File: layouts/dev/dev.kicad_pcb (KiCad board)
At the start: 6 copper layers, 32.5 x 59.6 mm, 85 parts

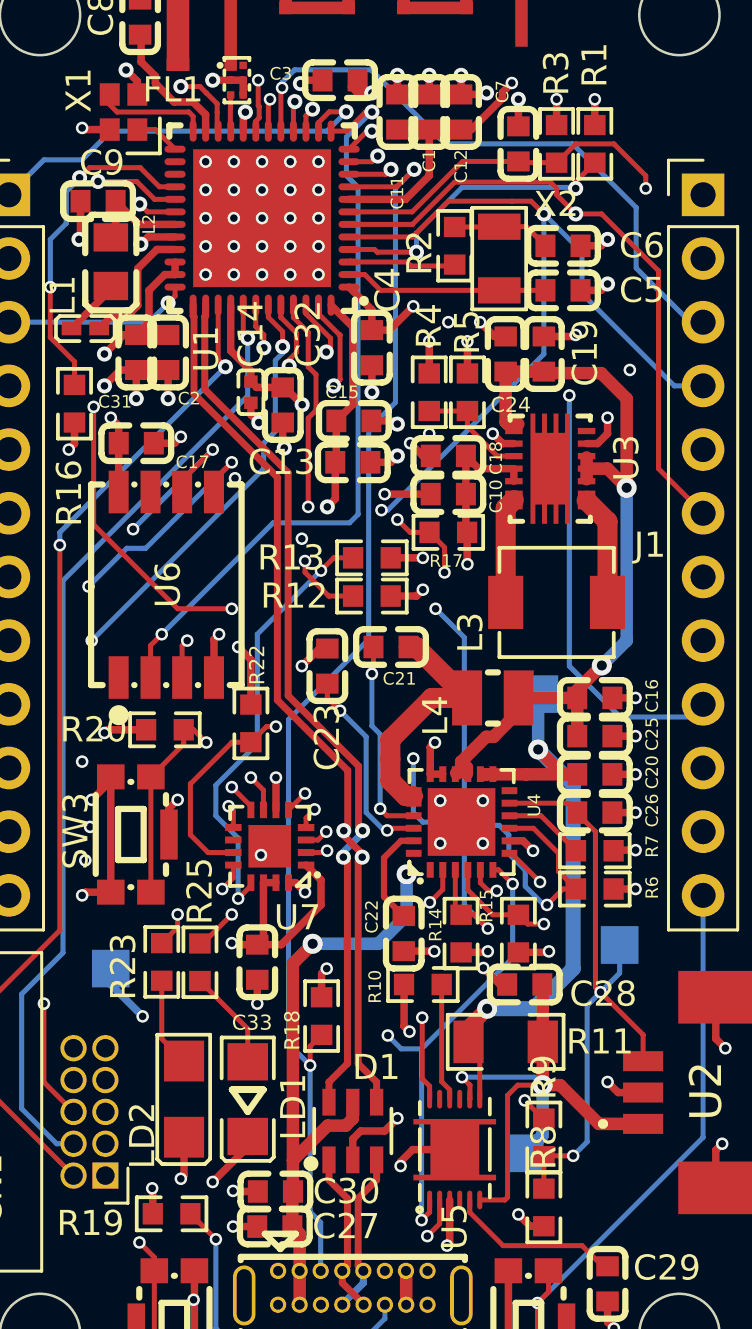
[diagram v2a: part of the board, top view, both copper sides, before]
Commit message: fix: stitch thermal pads by their real copper, not their bounding box
The TPS63020 and BQ27441 exposed pads were never stitched, and for the
whole project the tool reported them as "0.01 x 0.01 placeholders, not
thermal pads". That reading was wrong. Both are custom pads: 0.01 x 0.01 is
the anchor size and the real shape lives in the primitives. Measured on the
board they are 1.58 x 4.40 mm (6.95 mm2) and 3.30 x 2.45 mm (8.09 mm2),
both on F.Cu with paste and both on GND. The footprints were fine all
along; the tool could not see them because it read GetSizeX/GetSizeY.

Reading the bounding box instead fixes the detection and breaks two other
things, both of which surfaced immediately:

* the grid was computed in pad-local coordinates and then rotated, while
  the bounding box is already in board coordinates. On U3, rotated -90
  degrees, the axes swapped and two of four vias landed outside the pad,
  among the converter's lead pads.
* a bounding box is a rectangle and these pads are not. The BQ27441 pad is
  a T: a 2.0 x 1.95 mm centre bar plus two vertical strips 0.22 mm wide,
  where a 0.5 mm via can never fit. The TPS63020 pad is a comb. Gridding
  the rectangle puts vias on bare laminate.

So placement now works from the copper itself: candidates on a 0.1 mm
raster over the bounding box, each tested for whether the whole via -
centre and four points on its circumference - sits inside the pad polygon,
then picked greedily from the centre outwards with the pitch as the only
spacing rule.

The first run of that produced 18 shorts. A through via also pierces In2,
In3 and B.Cu, and the board had SD_CLK, SD_MISO, SD_MOSI, PB6, CHG_CE,
CHG_PG and GAUGE_INT routed under those parts. Every candidate is now also
checked against foreign copper on every layer, and the report says how many
positions that blocked - 673 under the MCU alone, which is why its grid
dropped from 27 vias to 19.

Zone filling moved into board_setup. The script adds and deletes vias, and
a pour fill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
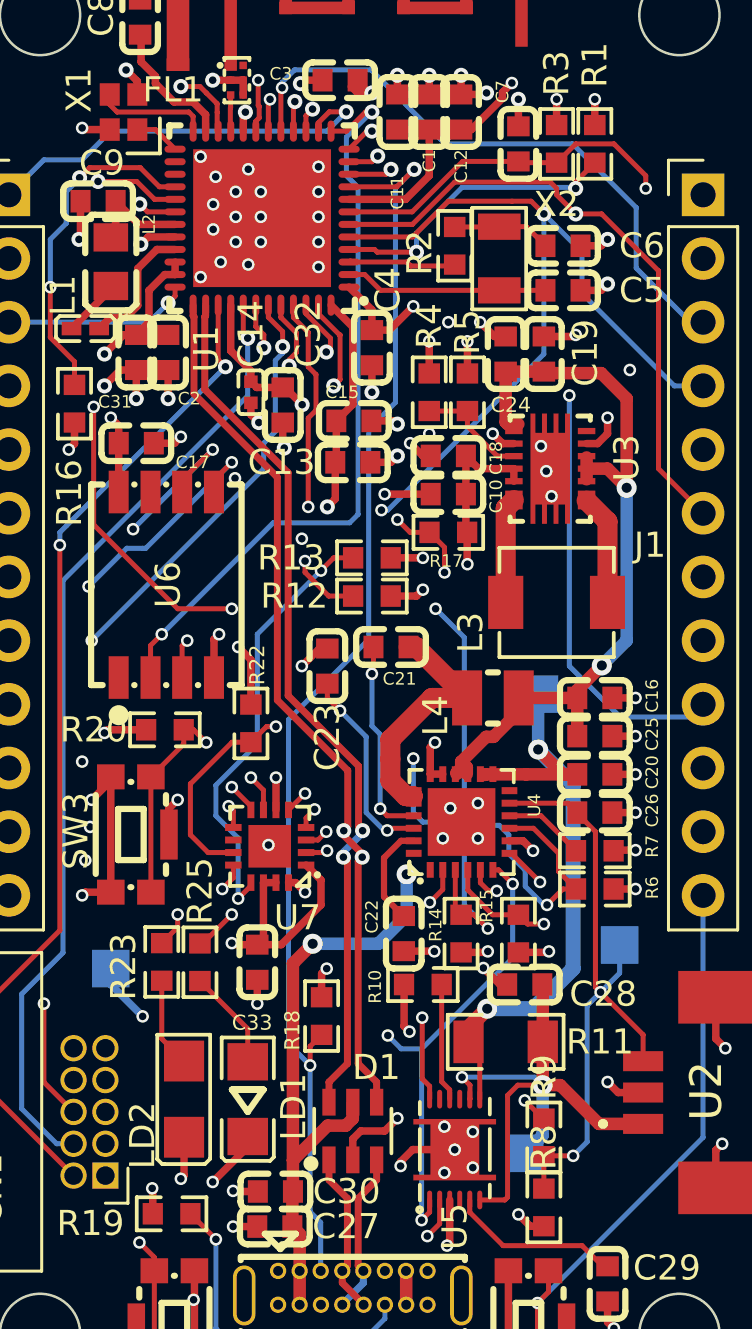
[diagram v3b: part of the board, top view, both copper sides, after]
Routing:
- net GND: vias 97 -> 99

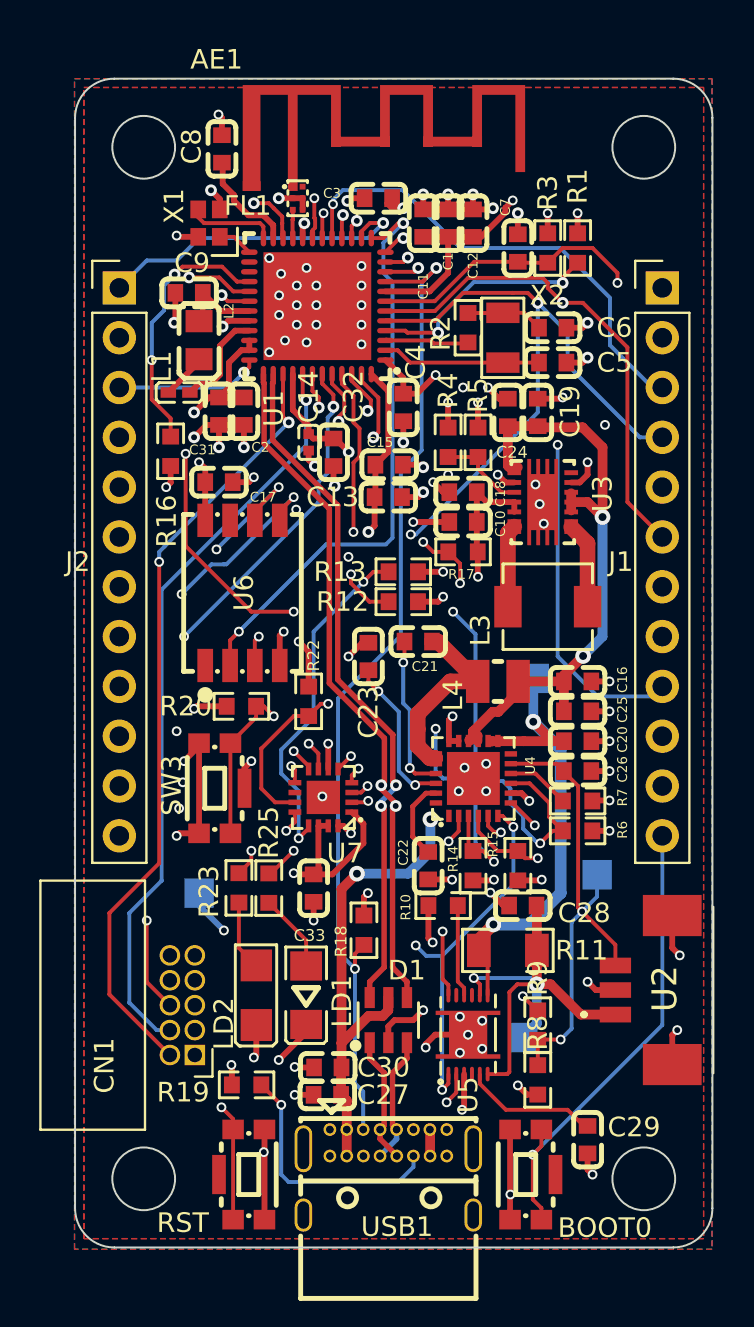
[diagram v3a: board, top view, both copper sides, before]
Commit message: feat: grow the board 1 mm upward and make the pours connect to pads
Two findings drove this, and the second one explains four unconnected
ground items at once.

The pours were set to ZONE_CONNECTION_NONE - all six of them, including the
In1 ground plane and the In4 power plane. A pour in that mode keeps
clearance from pads of its own net, so every ground pad without an explicit
track or via to it was left floating: the antenna's shorting stub, which is
the entire operating principle of an inverted-F; the MLPF's ground; and the
shields of both buttons. nowa_wylewka() has always set FULL, but set_zones
never corrected the pours it found, and that is the gap.

They are now forced to THT_THERMAL rather than FULL: solid for SMD pads,
thermal spokes for through-hole. This board is hand-soldered and a solid
ground connection on a header pin sinks heat faster than an iron delivers
it. F.Cu fragmentation dropped from 70 islands to 56.

Three islands still have no path to the plane - the antenna stub and the
two button shields. Each island is the pad itself with routing crowding it,
so the pour cannot physically reach, and none is large enough to hold a
0.5 mm via with clearance: 0.90 x 0.50, 0.71 x 1.89 and 0.59 x 1.89 against
the 0.80 mm a via needs in both axes. That is copper to be moved by hand,
not a setting.

The 1 mm comes off the top edge: BOARD_Y_MM 3.30 -> 2.30 with the height
59.60 -> 60.60, so the bottom edge and everything already placed stay put
and the space appears where it was needed. The top mounting holes follow to
y 5.80, the bottom pair stays at 59.40. For the antenna this is noise - the
counterpoise grows 1.7 % and was already twice a quarter wave at 2.45 GHz.

Keepout geometry was left alone after checking it: its lower edge sits
0.25 mm above the feed deliberately, because the two towers drop below it
into ground, which is where the shorting via belongs. The comment at
ANTENA_KEEPOUT_MM said so all along. The reason no via is there is simply
that the 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
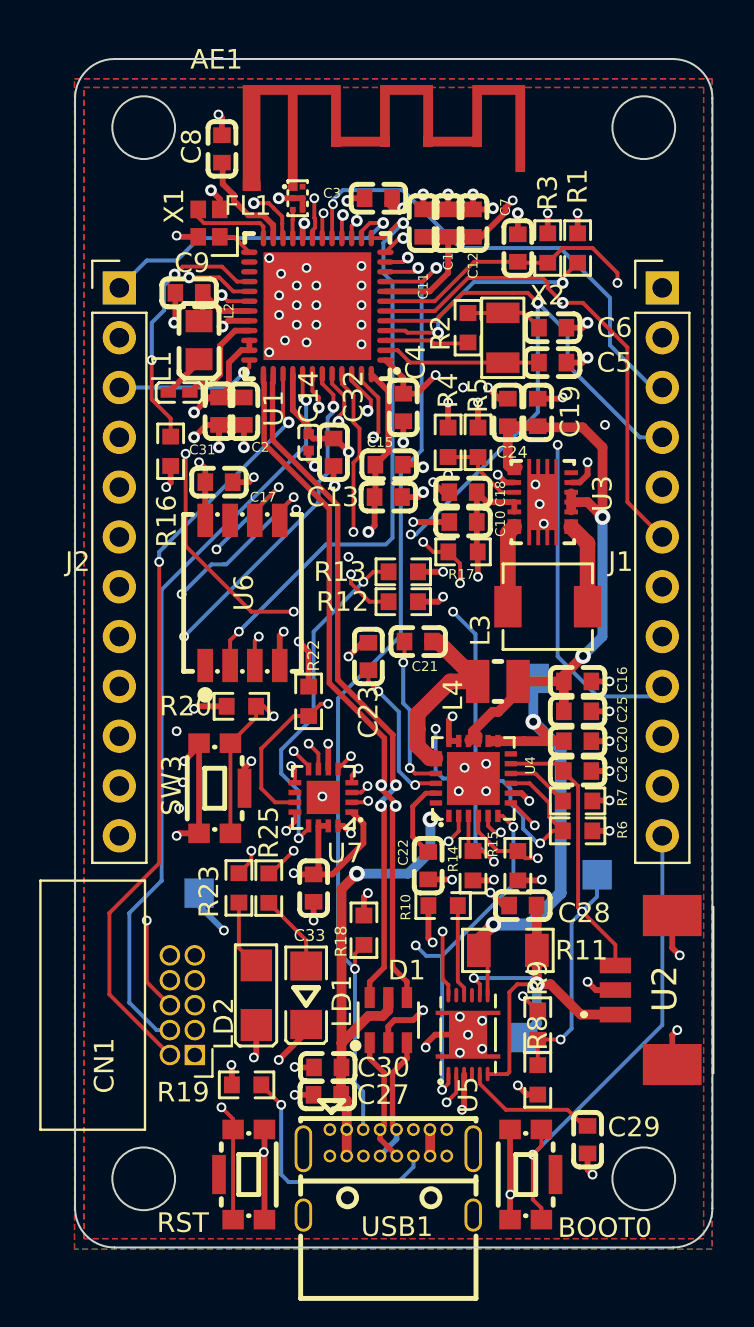
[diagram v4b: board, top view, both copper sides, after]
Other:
- board size 32.5 x 59.6 mm -> 32.5 x 60.6 mm

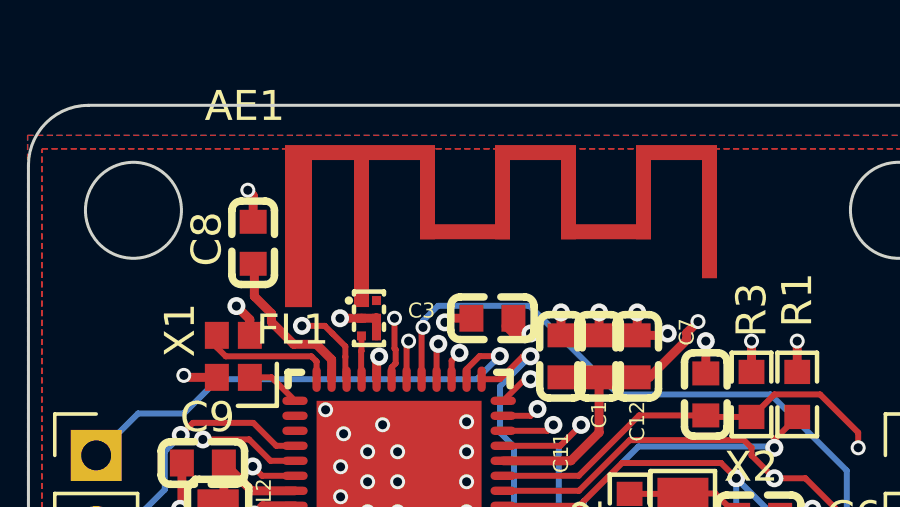
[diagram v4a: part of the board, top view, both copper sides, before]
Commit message: fix: give the antenna's shorting stub somewhere to land
The inverted-F had no DC path from its radiator to ground, which is not a
detail - the short to ground is the entire operating principle. Without it
the structure is a piece of copper at an undefined impedance.

The cause was dimensional. The comment at ANTENA_KEEPOUT_MM has always said
the two towers drop below the keepout into ground, "tam laduje przelotka
zwierajaca", so a shorting via was part of the design from the start. It was
never placed because it never could be: the stub foot from AN043 Table 1 is
0.90 x 0.50 mm and a 0.5 mm via with clearance needs 0.80 mm in both axes.

The footprint gains one rectangle that is not in Table 1: 1.10 x 1.10 mm
under the stub foot, at local (-2.10, +0.75) so it overlaps the foot and
merges with it. It sits below the keepout, already in ground territory, so
it is not part of the resonant structure - the note's warning that "small
changes of the antenna dimensions may have large impact on the performance"
is respected because no dimension from Table 1 was touched.

It started at 1.60 x 1.50 and had to come down to 1.10 x 1.10: at the larger
size it collided with the +3V3 tracks running left of the stub. 0.55 mm from
centre to edge against the 0.40 a via needs.

The antenna moved up 0.50 mm, not the full millimetre the new outline
offered. A full millimetre put its top copper exactly on the board edge,
against a 0.5 mm copper-to-edge rule, and brought back the three edge
violations the outline change had just removed. Half a millimetre is enough:
the MLPF now clears the antenna's shadow and its ground pad reaches the
pour. The feed, previously butted pad to pad, gets a 0.53 mm run at the RF
class width.

One pad came back from the rebuild with no net at all, which DRC reads as a
separate net and reported as three shorts against +3V3. board_setup now
heals that: in this footprint everything except the ANT pad is ground by
definition, so a netless pad gets GND.

Against th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
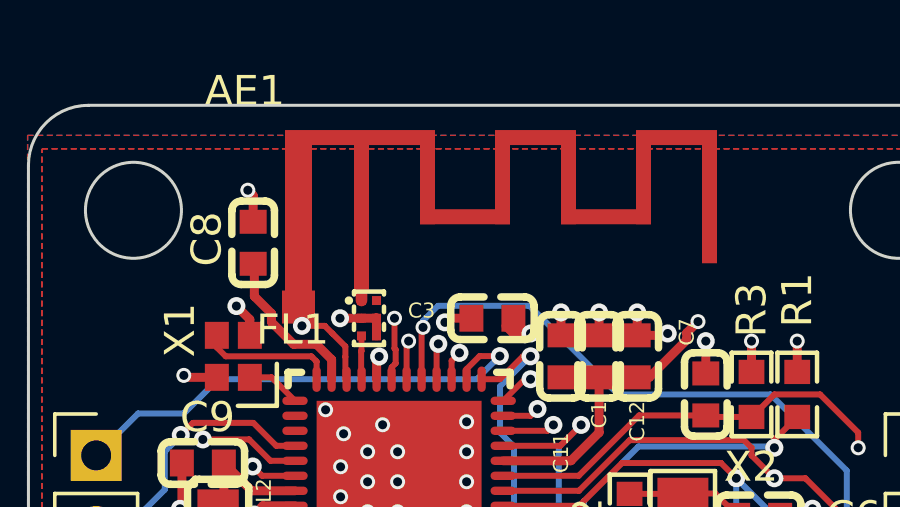
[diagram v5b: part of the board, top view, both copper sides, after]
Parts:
- moved AE1 0.50 mm to (19.5, 8.28)
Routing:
- net ANT: track 0.00 -> 0.53 mm
